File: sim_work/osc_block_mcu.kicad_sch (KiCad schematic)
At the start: 2 parts

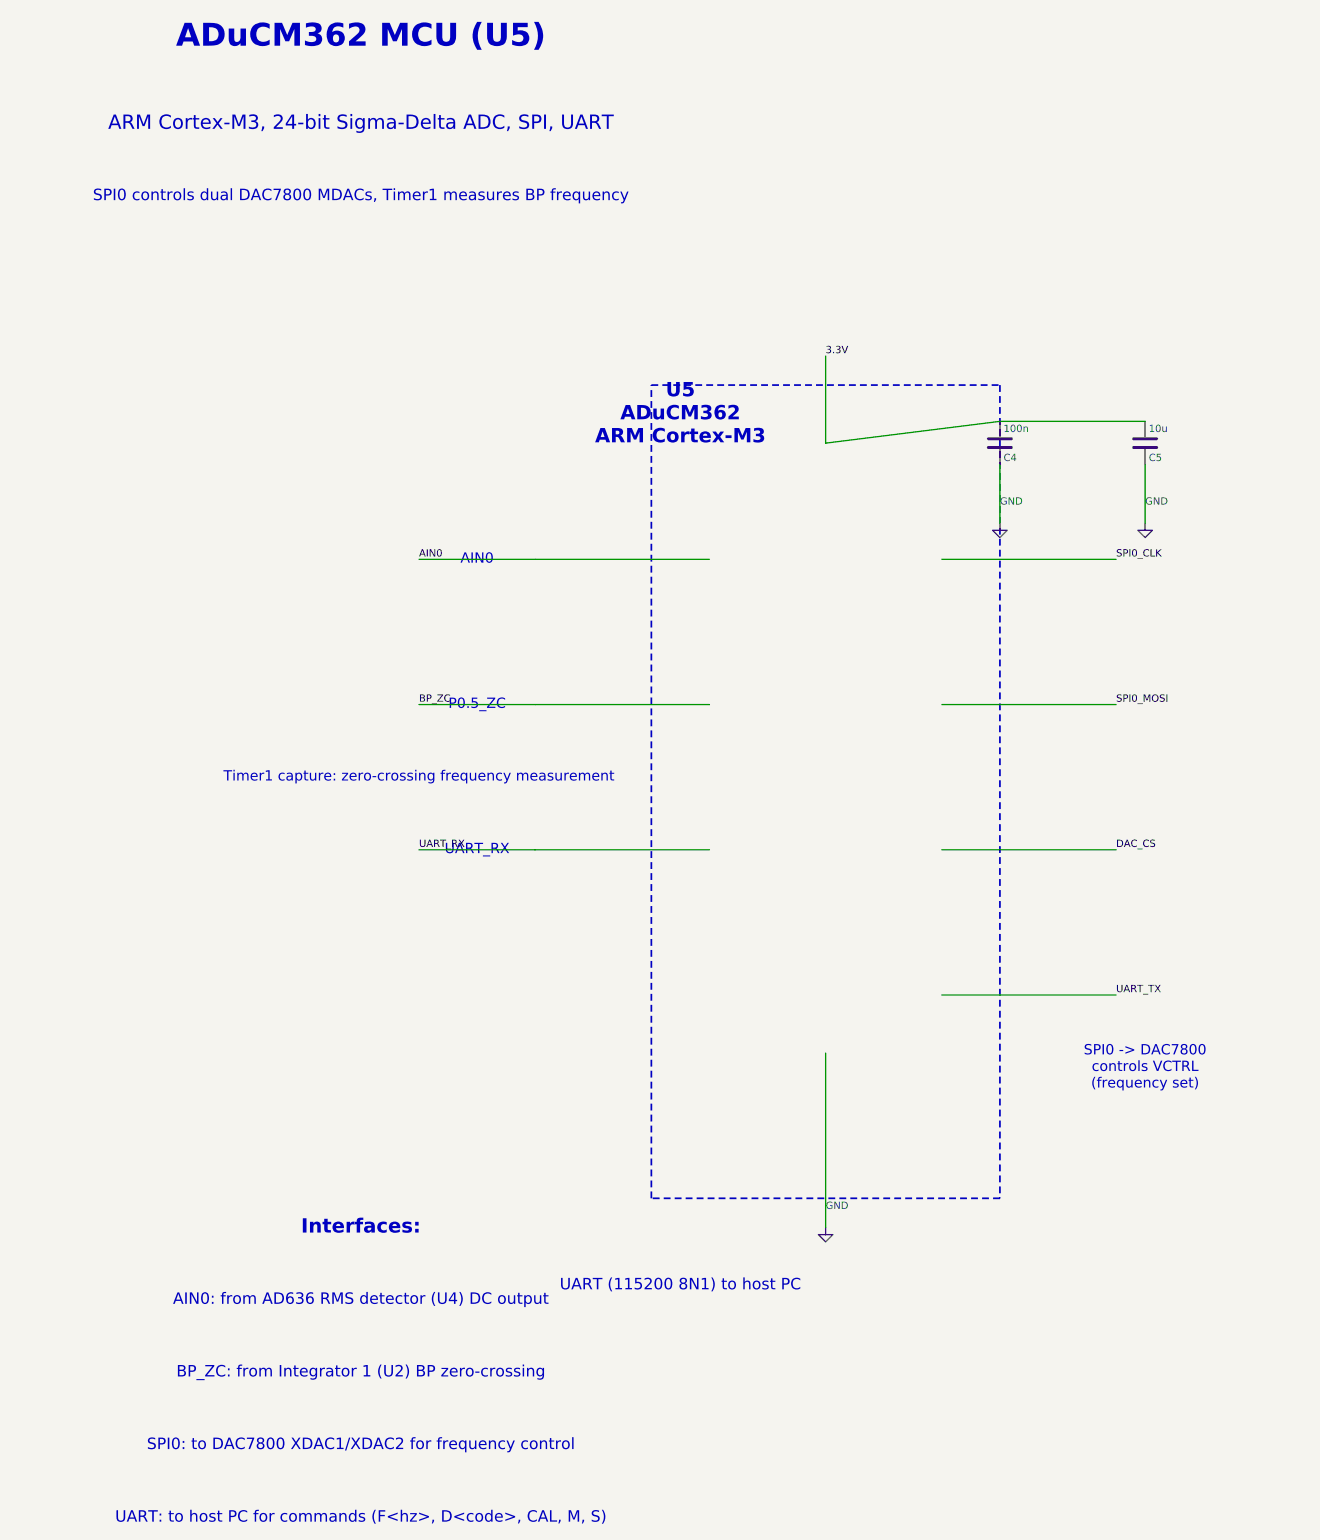
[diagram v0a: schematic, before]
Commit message: Fix schematic connections, add docs and repo portability
- Input filters: R rotation=90 (horizontal), ESD diode rotations fixed,
  junction dots at cathode-signal connection, wires to GND symbols
- Relay ladder: flyback diode rotation 270->90 (K top, A bottom)
- Electrometer/Mux TIA: 4 junction dots each at T-junctions
- AD636 RMS detector: proper IC box with pin labels replaces text-only
- Oscillator blocks: D_Zener symbol, L-shaped cathode routing
- TIA blocks: title/function annotations on all 5 blocks
- New: requirements.txt, docs/oscillator_guide.md
- D_Zener.kicad_sym added to bundled symbols/
- .gitignore updated for docs/ and requirements.txt
- README updated with pip install -r requirements.txt
- PROJECT.md session 9 changelog
- SimGUI builds clean (0 errors)

Co-Authored-By: Claude Opus 4.6 <noreply@anthropic.com>
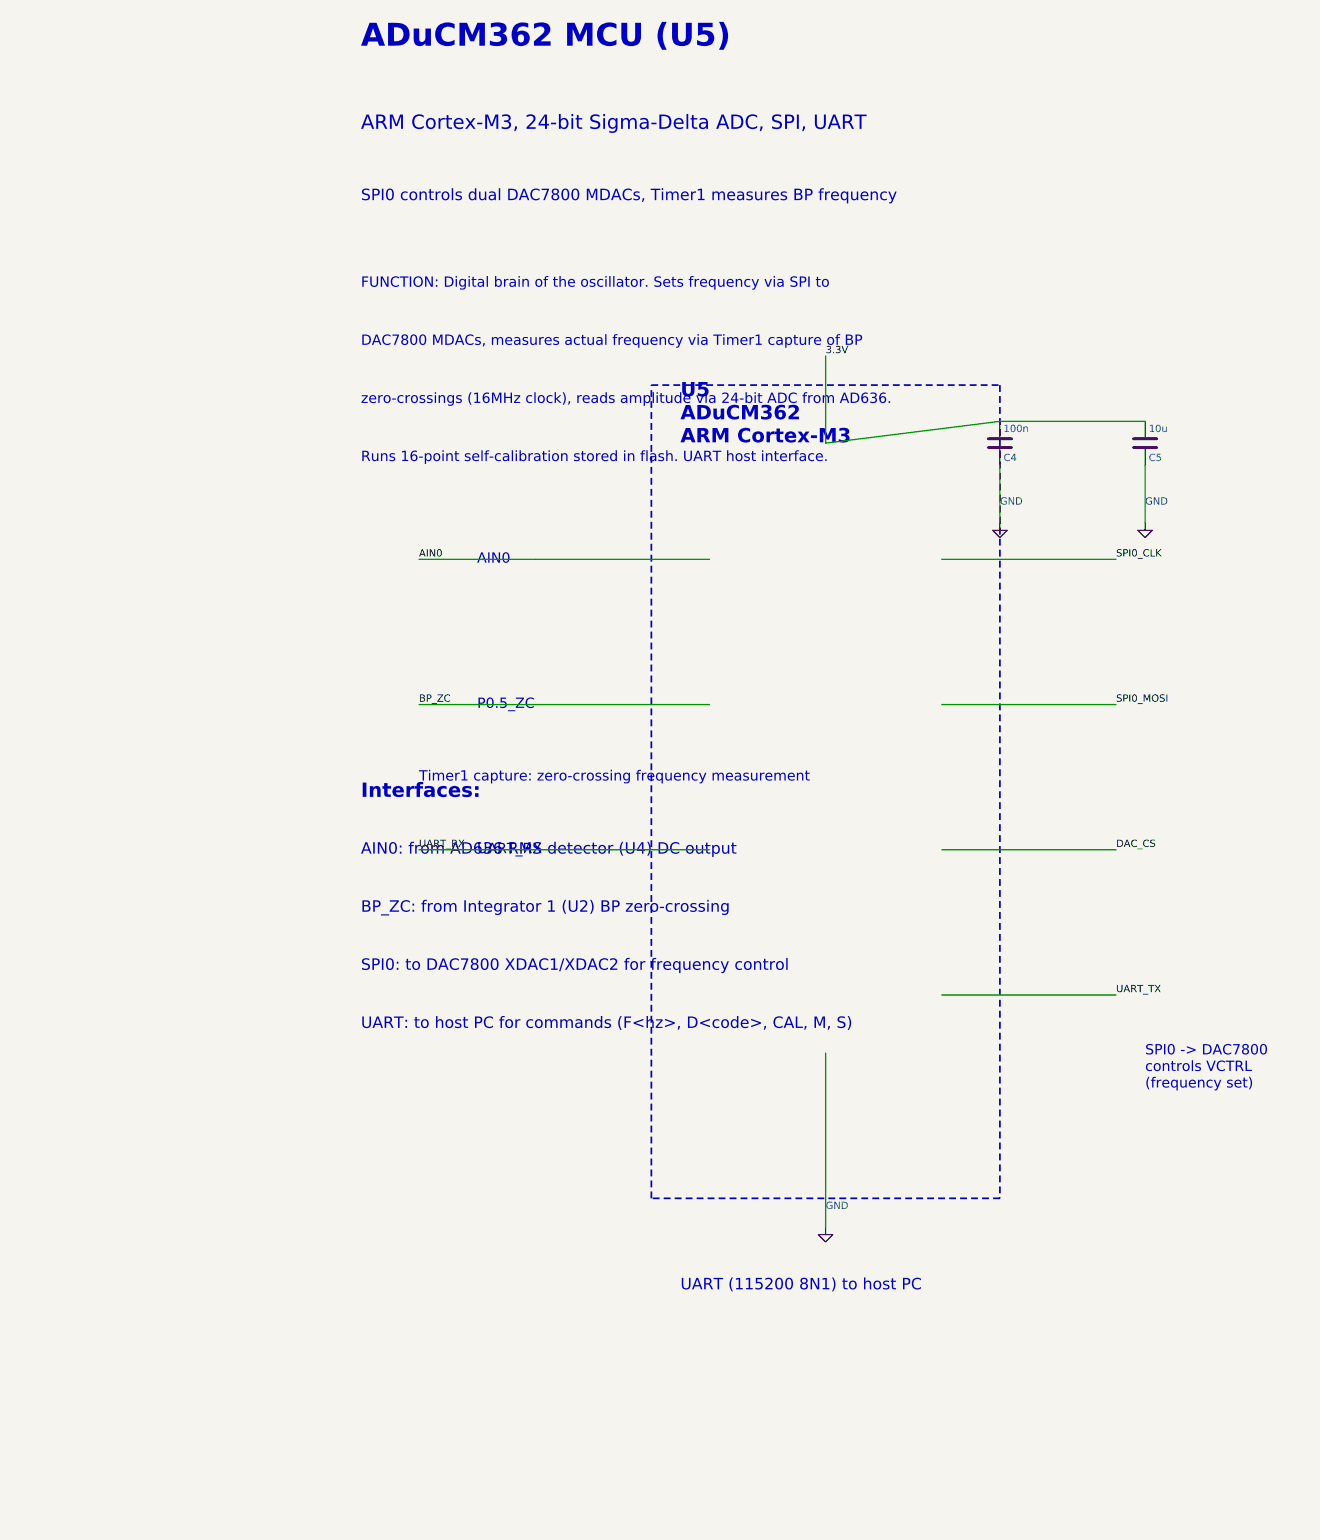
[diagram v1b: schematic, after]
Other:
- note added: "DAC7800 MDACs, measures actual frequency via Timer1 capture of BP"
- note added: "FUNCTION: Digital brain of the oscillator. Sets frequency via SPI to"
- note added: "Runs 16-point self-calibration stored in flash. UART host interface."
- note added: "zero-crossings (16MHz clock), reads amplitude via 24-bit ADC from AD636."
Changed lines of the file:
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@@
 		(instances
 			(project "Oscillator - ADuCM362 MCU"
-				(path "/444d1290-ba79-4edc-b1e7-1d06d0727c8c"
+				(path "/a226f6c2-ee07-43ef-bc26-c7f0ff72b899"
 					(reference "#PWR001")
 					(unit 1)
@@
 		(instances
 			(project "Oscillator - ADuCM362 MCU"
-				(path "/444d1290-ba79-4edc-b1e7-1d06d0727c8c"
+				(path "/a226f6c2-ee07-43ef-bc26-c7f0ff72b899"
 					(reference "C4")
 					(unit 1)
@@
 		(instances
 			(project "Oscillator - ADuCM362 MCU"
-				(path "/444d1290-ba79-4edc-b1e7-1d06d0727c8c"
+				(path "/a226f6c2-ee07-43ef-bc26-c7f0ff72b899"
 					(reference "#PWR002")
 					(unit 1)
@@
 		(instances
 			(project "Oscillator - ADuCM362 MCU"
-				(path "/444d1290-ba79-4edc-b1e7-1d06d0727c8c"
+				(path "/a226f6c2-ee07-43ef-bc26-c7f0ff72b899"
 					(reference "C5")
 					(unit 1)
@@
 		(instances
 			(project "Oscillator - ADuCM362 MCU"
-				(path "/444d1290-ba79-4edc-b1e7-1d06d0727c8c"
+				(path "/a226f6c2-ee07-43ef-bc26-c7f0ff72b899"
 					(reference "#PWR003")
 					(unit 1)
@@
 				(bold yes)
 			)
+			(justify left)
 		)
 	)
@@
 				(size 2.5 2.5)
 			)
+			(justify left)
 		)
 	)
@@
 				(size 2 2)
 			)
+			(justify left)
+		)
+	)
+	(text "FUNCTION: Digital brain of the oscillator. Sets frequency via SPI to"
+		(exclude_from_sim no)
+		(at 20.32 58.42 0.0000)
+		(effects
+			(font
+				(size 1.8 1.8)
+			)
+			(justify left)
+		)
+	)
+	(text "DAC7800 MDACs, measures actual frequency via Timer1 capture of BP"
+		(exclude_from_sim no)
+		(at 20.32 68.58 0.0000)
+		(effects
+			(font
+				(size 1.8 1.8)
+			)
+			(justify left)
+		)
+	)
+	(text "zero-crossings (16MHz clock), reads amplitude via 24-bit ADC from AD636."
+		(exclude_from_sim no)
+		(at 20.32 78.74 0.0000)
+		(effects
+			(font
+				(size 1.8 1.8)
+			)
+			(justify left)
+		)
+	)
+	(text "Runs 16-point self-calibration stored in flash. UART host interface."
+		(exclude_from_sim no)
+		(at 20.32 88.9 0.0000)
+		(effects
+			(font
+				(size 1.8 1.8)
+			)
+			(justify left)
 		)
 	)
@@
 				(bold yes)
 			)
+			(justify left)
 		)
 	)
@@
 				(size 1.8 1.8)
 			)
+			(justify left)
 		)
 	)
@@
 				(size 1.8 1.8)
 			)
+			(justify left)
 		)
 	)
@@
 				(size 1.8 1.8)
 			)
+			(justify left)
 		)
 	)
@@
 				(size 1.8 1.8)
 			)
+			(justify left)
 		)
 	)
@@
 				(size 2 2)
 			)
+			(justify left)
 		)
 	)
@@
 				(size 1.8 1.8)
 			)
+			(justify left)
 		)
 	)
 	(text "Interfaces:"
 		(exclude_from_sim no)
-		(at 20.32 223.52 0.0000)
+		(at 20.32 147.32 0.0000)
 		(effects
 			(font
@@
 				(bold yes)
 			)
+			(justify left)
 		)
 	)
 	(text "AIN0: from AD636 RMS detector (U4) DC output"
 		(exclude_from_sim no)
-		(at 20.32 236.22 0.0000)
+		(at 20.32 157.48 0.0000)
 		(effects
 			(font
 				(size 2 2)
 			)
+			(justify left)
 		)
 	)
 	(text "BP_ZC: from Integrator 1 (U2) BP zero-crossing"
 		(exclude_from_sim no)
-		(at 20.32 248.92 0.0000)
+		(at 20.32 167.64 0.0000)
 		(effects
 			(font
 				(size 2 2)
 			)
+			(justify left)
 		)
 	)
 	(text "SPI0: to DAC7800 XDAC1/XDAC2 for frequency control"
 		(exclude_from_sim no)
-		(at 20.32 261.62 0.0000)
+		(at 20.32 177.8 0.0000)
 		(effects
 			(font
 				(size 2 2)
 			)
+			(justify left)
 		)
 	)
 	(text "UART: to host PC for commands (F<hz>, D<code>, CAL, M, S)"
 		(exclude_from_sim no)
-		(at 20.32 274.32 0.0000)
+		(at 20.32 187.96 0.0000)
 		(effects
 			(font
 				(size 2 2)
 			)
-		)
-	)
+			(justify left)
+		)
+	)
